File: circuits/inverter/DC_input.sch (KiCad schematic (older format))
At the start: 0 parts

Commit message: Add more circuitry, add library content
AC current measurement
AC filter
AC switch
DC booster
DC input
Analog frontend
drivers
inverter
main controller
power supply

new components for:
standard library (e.g. relay)
AC current sensor acs722
voltage regulator LM317L

Footprints for:
AC relay
TO-220
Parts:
- added C? (x4): Capacitor, symbol Capacitor
- added L? (x2): Inductor, symbol Inductor
- added MB?: DC+_Terminal, symbol Plated_hole
- added MB?: DC-_Terminal, symbol Plated_hole
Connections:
- net labels added: DC+, DC-_Shunt+, Earth_Protective
- wire segments 0 -> 14
- no-connect marks 0 -> 1
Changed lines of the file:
@@
 EESchema Schematic File Version 2
+LIBS:lm317
 LIBS:kv30f
 LIBS:OSSI_standard_components
@@
 LIBS:lm4030
 LIBS:power
+LIBS:acs722
 LIBS:OSSI_MK_I-cache
 EELAYER 25 0
@@
 $Descr A4 11693 8268
 encoding utf-8
-Sheet 1 10
-Title ""
+Sheet 2 11
+Title "DC Input Terminals and Filter"
 Date ""
 Rev "0.1"
@@
 Comment4 ""
 $EndDescr
+$Comp
+L Plated_hole MB?
+U 1 1 56E6DE87
+P 2700 3000
+F 0 "MB?" H 2700 2850 60  0000 C CNN
+F 1 "DC+_Terminal" H 2710 3160 60  0000 C CNN
+F 2 "" H 2700 3000 60  0000 C CNN
+F 3 "" H 2700 3000 60  0000 C CNN
+	1    2700 3000
+	1    0    0    -1
+$EndComp
+$Comp
+L Plated_hole MB?
+U 1 1 56E6DFE4
+P 2700 4150
+F 0 "MB?" H 2700 4000 60  0000 C CNN
+F 1 "DC-_Terminal" H 2710 4310 60  0000 C CNN
+F 2 "" H 2700 4150 60  0000 C CNN
+F 3 "" H 2700 4150 60  0000 C CNN
+	1    2700 4150
+	1    0    0    -1
+$EndComp
+$Comp
+L Capacitor C?
+U 1 1 56E6E0C5
+P 4300 3250
+F 0 "C?" H 4300 3100 60  0000 C CNN
+F 1 "Capacitor" H 4315 3395 60  0000 C CNN
+F 2 "" H 4300 3250 60  0000 C CNN
+F 3 "" H 4300 3250 60  0000 C CNN
+F 4 "%" H 4300 3475 60  0000 C CNN "Tolerance"
+F 5 "M" H 4550 3450 60  0001 L CNN "Manufacturer"
+F 6 "P" H 4550 3350 60  0001 L CNN "Partnumber"
+	1    4300 3250
+	0    -1   1    0
+$EndComp
+$Comp
+L Capacitor C?
+U 1 1 56E6E157
+P 4300 3850
+F 0 "C?" H 4300 3700 60  0000 C CNN
+F 1 "Capacitor" H 4315 3995 60  0000 C CNN
+F 2 "" H 4300 3850 60  0000 C CNN
+F 3 "" H 4300 3850 60  0000 C CNN
+F 4 "%" H 4300 4075 60  0000 C CNN "Tolerance"
+F 5 "M" H 4550 4050 60  0001 L CNN "Manufacturer"
+F 6 "P" H 4550 3950 60  0001 L CNN "Partnumber"
+	1    4300 3850
+	0    -1   1    0
+$EndComp
+$Comp
+L Inductor L?
+U 1 1 56E6E196
+P 5250 3000
+F 0 "L?" H 5250 2850 60  0000 C CNN
+F 1 "Inductor" H 5250 2950 60  0000 C CNN
+F 2 "" H 5250 3000 60  0000 C CNN
+F 3 "" H 5250 3000 60  0000 C CNN
+F 4 "M" H 5425 3200 60  0001 L CNN "Manufacturer"
+F 5 "P" H 5425 3100 60  0001 L CNN "Partnumber"
+	1    5250 3000
+	1    0    0    -1
+$EndComp
+$Comp
+L Inductor L?
+U 1 1 56E6E24A
+P 5250 4150
+F 0 "L?" H 5250 4000 60  0000 C CNN
+F 1 "Inductor" H 5250 4100 60  0000 C CNN
+F 2 "" H 5250 4150 60  0000 C CNN
+F 3 "" H 5250 4150 60  0000 C CNN
+F 4 "M" H 5425 4350 60  0001 L CNN "Manufacturer"
+F 5 "P" H 5425 4250 60  0001 L CNN "Partnumber"
+	1    5250 4150
+	1    0    0    -1
+$EndComp
+$Comp
+L Capacitor C?
+U 1 1 56E6E29F
+P 6250 3250
+F 0 "C?" H 6250 3100 60  0000 C CNN
+F 1 "Capacitor" H 6265 3395 60  0000 C CNN
+F 2 "" H 6250 3250 60  0000 C CNN
+F 3 "" H 6250 3250 60  0000 C CNN
+F 4 "%" H 6250 3475 60  0000 C CNN "Tolerance"
+F 5 "M" H 6500 3450 60  0001 L CNN "Manufacturer"
+F 6 "P" H 6500 3350 60  0001 L CNN "Partnumber"
+	1    6250 3250
+	0    -1   1    0
+$EndComp
+$Comp
+L Capacitor C?
+U 1 1 56E6E320
+P 6250 3800
+F 0 "C?" H 6250 3650 60  0000 C CNN
+F 1 "Capacitor" H 6265 3945 60  0000 C CNN
+F 2 "" H 6250 3800 60  0000 C CNN
+F 3 "" H 6250 3800 60  0000 C CNN
+F 4 "%" H 6250 4025 60  0000 C CNN "Tolerance"
+F 5 "M" H 6500 4000 60  0001 L CNN "Manufacturer"
+F 6 "P" H 6500 3900 60  0001 L CNN "Partnumber"
+	1    6250 3800
+	0    -1   1    0
+$EndComp
+Wire Wire Line
+	2700 4150 5000 4150
+Wire Wire Line
+	5500 4150 8000 4150
+Text HLabel 8000 3000 2    60   Output ~ 0
+DC+
+Wire Wire Line
+	5500 3000 8000 3000
+Wire Wire Line
+	6250 3150 6250 3000
+Connection ~ 6250 3000
+Wire Wire Line
+	6250 3350 6250 3700
+Wire Wire Line
+	6250 3900 6250 4150
+Connection ~ 6250 4150
+Wire Wire Line
+	2700 3000 5000 3000
+Wire Wire Line
+	4300 3150 4300 3000
+Connection ~ 4300 3000
+Wire Wire Line
+	4300 3350 4300 3750
+Wire Wire Line
+	4300 3950 4300 4150
+Connection ~ 4300 4150
+$Comp
+L Earth_Protective #PWR?
+U 1 1 56E6E7AC
+P 4750 3600
+F 0 "#PWR?" H 5000 3350 50  0001 C CNN
+F 1 "Earth_Protective" H 5200 3450 50  0001 C CNN
+F 2 "" H 4750 3500 50  0000 C CNN
+F 3 "" H 4750 3500 50  0000 C CNN
+	1    4750 3600
+	1    0    0    -1
+$EndComp
+Wire Wire Line
+	4750 3600 4750 3550
+Wire Wire Line
+	4750 3550 4300 3550
+Connection ~ 4300 3550
+$Comp
+L Earth_Protective #PWR?
+U 1 1 56E6EC38
+P 6700 3600
+F 0 "#PWR?" H 6950 3350 50  0001 C CNN
+F 1 "Earth_Protective" H 7150 3450 50  0001 C CNN
+F 2 "" H 6700 3500 50  0000 C CNN
+F 3 "" H 6700 3500 50  0000 C CNN
+	1    6700 3600
+	1    0    0    -1
+$EndComp
+Wire Wire Line
+	6700 3600 6700 3550
+Wire Wire Line
+	6700 3550 6250 3550
+Connection ~ 6250 3550
+NoConn ~ 6050 3600
+Text HLabel 8000 4150 2    60   Input ~ 0
+DC-_Shunt+
 $EndSCHEMATC

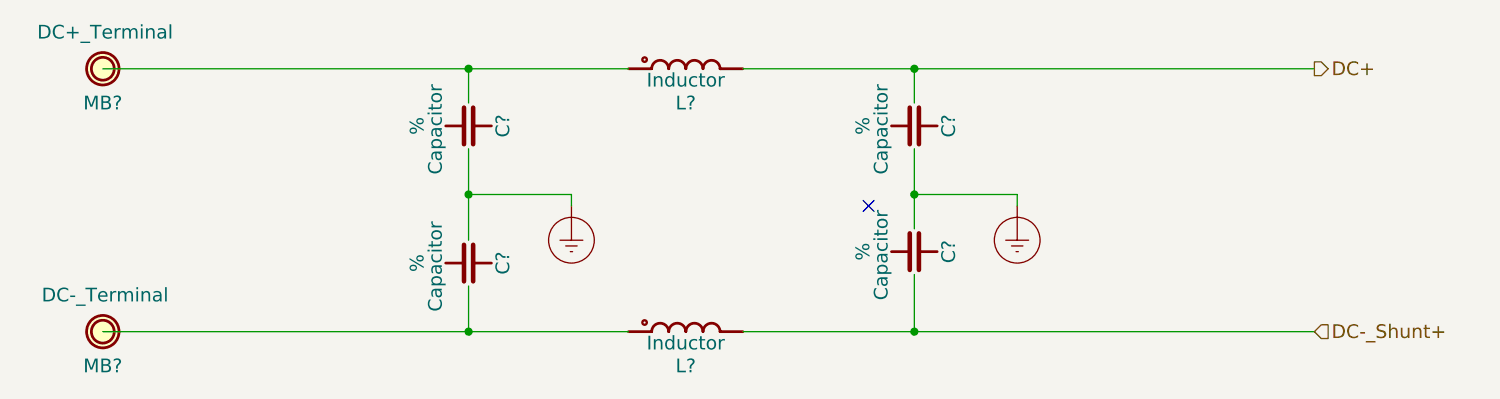
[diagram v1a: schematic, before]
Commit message: Updates all schematic pages to current components
all components are replaced with the current component library parts
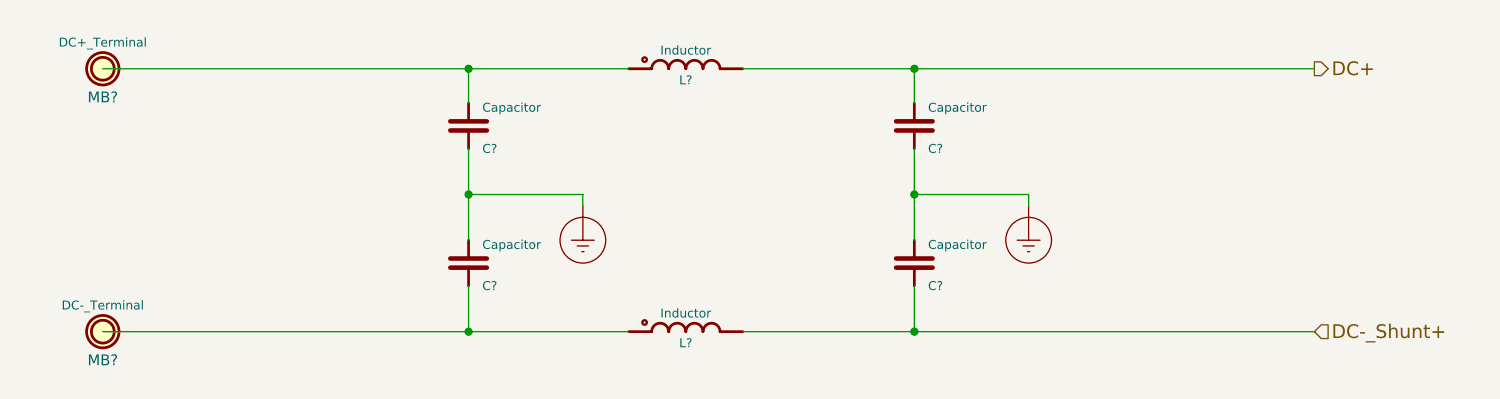
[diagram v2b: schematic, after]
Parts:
- removed C? (x4): Capacitor, symbol Capacitor
- removed L? (x2): Inductor, symbol Inductor
- removed MB?: DC+_Terminal, symbol Plated_hole
- removed MB?: DC-_Terminal, symbol Plated_hole
- added C? (x4): Capacitor, symbol Capacitor
- added L? (x2): Inductor, symbol Inductor
- added MB?: DC+_Terminal, symbol Plated_hole
- added MB?: DC-_Terminal, symbol Plated_hole
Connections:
- wire segments 14 -> 20
- no-connect marks 1 -> 0
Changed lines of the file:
@@
 LIBS:connectors
 LIBS:lm4030
-LIBS:power
 LIBS:acs722
 LIBS:OSSI_MK_I-cache
@@
 Comment4 ""
 $EndDescr
+Wire Wire Line
+	2700 4150 4300 4150
+Wire Wire Line
+	4300 4150 5000 4150
+Wire Wire Line
+	5500 4150 6250 4150
+Wire Wire Line
+	6250 4150 8000 4150
+Text HLabel 8000 3000 2    60   Output ~ 0
+DC+
+Wire Wire Line
+	5500 3000 6250 3000
+Wire Wire Line
+	6250 3000 8000 3000
+Wire Wire Line
+	6250 3150 6250 3000
+Connection ~ 6250 3000
+Wire Wire Line
+	6250 3350 6250 3550
+Wire Wire Line
+	6250 3550 6250 3750
+Wire Wire Line
+	6250 3950 6250 4150
+Connection ~ 6250 4150
+Wire Wire Line
+	2700 3000 4300 3000
+Wire Wire Line
+	4300 3000 5000 3000
+Wire Wire Line
+	4300 3150 4300 3000
+Connection ~ 4300 3000
+Wire Wire Line
+	4300 3350 4300 3550
+Wire Wire Line
+	4300 3550 4300 3750
+Wire Wire Line
+	4300 3950 4300 4150
+Connection ~ 4300 4150
+$Comp
+L Earth_Protective #PWR01
+U 1 1 56E6E7AC
+P 4800 3600
+F 0 "#PWR01" H 5050 3350 50  0001 C CNN
+F 1 "Earth_Protective" H 5250 3450 50  0001 C CNN
+F 2 "" H 4800 3500 50  0000 C CNN
+F 3 "" H 4800 3500 50  0000 C CNN
+	1    4800 3600
+	1    0    0    -1
+$EndComp
+Wire Wire Line
+	4800 3600 4800 3550
+Wire Wire Line
+	4800 3550 4300 3550
+Connection ~ 4300 3550
+$Comp
+L Earth_Protective #PWR02
+U 1 1 56E6EC38
+P 6750 3600
+F 0 "#PWR02" H 7000 3350 50  0001 C CNN
+F 1 "Earth_Protective" H 7200 3450 50  0001 C CNN
+F 2 "" H 6750 3500 50  0000 C CNN
+F 3 "" H 6750 3500 50  0000 C CNN
+	1    6750 3600
+	1    0    0    -1
+$EndComp
+Wire Wire Line
+	6750 3600 6750 3550
+Wire Wire Line
+	6750 3550 6250 3550
+Connection ~ 6250 3550
+Text HLabel 8000 4150 2    60   Input ~ 0
+DC-_Shunt+
+$Comp
+L Capacitor C?
+U 1 1 58D7EC0B
+P 4300 3250
+F 0 "C?" H 4360 3150 39  0000 L CNN
+F 1 "Capacitor" H 4360 3330 39  0000 L CNN
+F 2 "" H 4250 3160 39  0001 R CNN
+F 3 "" V 4300 3250 60  0000 C CNN
+F 4 "%" H 4250 3330 39  0001 R CNN "Tolerance"
+F 5 "M" H 4360 3445 35  0001 L CNN "Manufacturer"
+F 6 "P" H 4360 3390 35  0001 L CNN "Partnumber"
+F 7 "S" H 4360 3505 35  0001 L CNN "Supplier"
+F 8 "O.No." H 4360 3555 35  0001 L CNN "Order No."
+	1    4300 3250
+	1    0    0    -1
+$EndComp
+$Comp
+L Capacitor C?
+U 1 1 58D7EC75
+P 4300 3850
+F 0 "C?" H 4360 3750 39  0000 L CNN
+F 1 "Capacitor" H 4360 3930 39  0000 L CNN
+F 2 "" H 4250 3760 39  0001 R CNN
+F 3 "" V 4300 3850 60  0000 C CNN
+F 4 "%" H 4250 3930 39  0001 R CNN "Tolerance"
+F 5 "M" H 4360 4045 35  0001 L CNN "Manufacturer"
+F 6 "P" H 4360 3990 35  0001 L CNN "Partnumber"
+F 7 "S" H 4360 4105 35  0001 L CNN "Supplier"
+F 8 "O.No." H 4360 4155 35  0001 L CNN "Order No."
+	1    4300 3850
+	1    0    0    -1
+$EndComp
+$Comp
+L Capacitor C?
+U 1 1 58D7ED36
+P 6250 3250
+F 0 "C?" H 6310 3150 39  0000 L CNN
+F 1 "Capacitor" H 6310 3330 39  0000 L CNN
+F 2 "" H 6200 3160 39  0001 R CNN
+F 3 "" V 6250 3250 60  0000 C CNN
+F 4 "%" H 6200 3330 39  0001 R CNN "Tolerance"
+F 5 "M" H 6310 3445 35  0001 L CNN "Manufacturer"
+F 6 "P" H 6310 3390 35  0001 L CNN "Partnumber"
+F 7 "S" H 6310 3505 35  0001 L CNN "Supplier"
+F 8 "O.No." H 6310 3555 35  0001 L CNN "Order No."
+	1    6250 3250
+	1    0    0    -1
+$EndComp
+$Comp
+L Capacitor C?
+U 1 1 58D7EDAD
+P 6250 3850
+F 0 "C?" H 6310 3750 39  0000 L CNN
+F 1 "Capacitor" H 6310 3930 39  0000 L CNN
+F 2 "" H 6200 3760 39  0001 R CNN
+F 3 "" V 6250 3850 60  0000 C CNN
+F 4 "%" H 6200 3930 39  0001 R CNN "Tolerance"
+F 5 "M" H 6310 4045 35  0001 L CNN "Manufacturer"
+F 6 "P" H 6310 3990 35  0001 L CNN "Partnumber"
+F 7 "S" H 6310 4105 35  0001 L CNN "Supplier"
+F 8 "O.No." H 6310 4155 35  0001 L CNN "Order No."
+	1    6250 3850
+	1    0    0    -1
+$EndComp
+$Comp
+L Inductor L?
+U 1 1 58D7EE81
+P 5250 3000
+F 0 "L?" H 5250 2950 39  0000 C CNN
+F 1 "Inductor" H 5250 3080 39  0000 C CNN
+F 2 "" H 5250 3155 35  0000 C CNN
+F 3 "" H 5250 3000 60  0000 C CNN
+F 4 "M" H 5420 3185 35  0001 L CNN "Manufacturer"
+F 5 "P" H 5420 3130 35  0001 L CNN "Partnumber"
+F 6 "S" H 5420 3240 35  0001 L CNN "Supplier"
+F 7 "O.No." H 5420 3290 35  0001 L CNN "Order No."
+	1    5250 3000
+	1    0    0    -1
+$EndComp
+$Comp
+L Inductor L?
+U 1 1 58D7EEE9
+P 5250 4150
+F 0 "L?" H 5250 4100 39  0000 C CNN
+F 1 "Inductor" H 5250 4230 39  0000 C CNN
+F 2 "" H 5250 4305 35  0000 C CNN
+F 3 "" H 5250 4150 60  0000 C CNN
+F 4 "M" H 5420 4335 35  0001 L CNN "Manufacturer"
+F 5 "P" H 5420 4280 35  0001 L CNN "Partnumber"
+F 6 "S" H 5420 4390 35  0001 L CNN "Supplier"
+F 7 "O.No." H 5420 4440 35  0001 L CNN "Order No."
+	1    5250 4150
+	1    0    0    -1
+$EndComp
 $Comp
 L Plated_hole MB?
-U 1 1 56E6DE87
+U 1 1 58E38B7C
 P 2700 3000
-F 0 "MB?" H 2700 2850 60  0000 C CNN
-F 1 "DC+_Terminal" H 2710 3160 60  0000 C CNN
+F 0 "MB?" H 2700 2875 47  0000 C CNN
+F 1 "DC+_Terminal" H 2700 3115 39  0000 C CNN
 F 2 "" H 2700 3000 60  0000 C CNN
 F 3 "" H 2700 3000 60  0000 C CNN
@@
 $Comp
 L Plated_hole MB?
-U 1 1 56E6DFE4
+U 1 1 58E38E08
 P 2700 4150
-F 0 "MB?" H 2700 4000 60  0000 C CNN
-F 1 "DC-_Terminal" H 2710 4310 60  0000 C CNN
+F 0 "MB?" H 2700 4025 47  0000 C CNN
+F 1 "DC-_Terminal" H 2700 4265 39  0000 C CNN
 F 2 "" H 2700 4150 60  0000 C CNN
 F 3 "" H 2700 4150 60  0000 C CNN
@@
 	1    0    0    -1
 $EndComp
-$Comp
-L Capacitor C?
-U 1 1 56E6E0C5
-P 4300 3250
-F 0 "C?" H 4300 3100 60  0000 C CNN
-F 1 "Capacitor" H 4315 3395 60  0000 C CNN
-F 2 "" H 4300 3250 60  0000 C CNN
-F 3 "" H 4300 3250 60  0000 C CNN
-F 4 "%" H 4300 3475 60  0000 C CNN "Tolerance"
-F 5 "M" H 4550 3450 60  0001 L CNN "Manufacturer"
-F 6 "P" H 4550 3350 60  0001 L CNN "Partnumber"
-	1    4300 3250
-	0    -1   1    0
-$EndComp
-$Comp
-L Capacitor C?
-U 1 1 56E6E157
-P 4300 3850
-F 0 "C?" H 4300 3700 60  0000 C CNN
-F 1 "Capacitor" H 4315 3995 60  0000 C CNN
-F 2 "" H 4300 3850 60  0000 C CNN
-F 3 "" H 4300 3850 60  0000 C CNN
-F 4 "%" H 4300 4075 60  0000 C CNN "Tolerance"
-F 5 "M" H 4550 4050 60  0001 L CNN "Manufacturer"
-F 6 "P" H 4550 3950 60  0001 L CNN "Partnumber"
-	1    4300 3850
-	0    -1   1    0
-$EndComp
-$Comp
-L Inductor L?
-U 1 1 56E6E196
-P 5250 3000
-F 0 "L?" H 5250 2850 60  0000 C CNN
-F 1 "Inductor" H 5250 2950 60  0000 C CNN
-F 2 "" H 5250 3000 60  0000 C CNN
-F 3 "" H 5250 3000 60  0000 C CNN
-F 4 "M" H 5425 3200 60  0001 L CNN "Manufacturer"
-F 5 "P" H 5425 3100 60  0001 L CNN "Partnumber"
-	1    5250 3000
-	1    0    0    -1
-$EndComp
-$Comp
-L Inductor L?
-U 1 1 56E6E24A
-P 5250 4150
-F 0 "L?" H 5250 4000 60  0000 C CNN
-F 1 "Inductor" H 5250 4100 60  0000 C CNN
-F 2 "" H 5250 4150 60  0000 C CNN
-F 3 "" H 5250 4150 60  0000 C CNN
-F 4 "M" H 5425 4350 60  0001 L CNN "Manufacturer"
-F 5 "P" H 5425 4250 60  0001 L CNN "Partnumber"
-	1    5250 4150
-	1    0    0    -1
-$EndComp
-$Comp
-L Capacitor C?
-U 1 1 56E6E29F
-P 6250 3250
-F 0 "C?" H 6250 3100 60  0000 C CNN
-F 1 "Capacitor" H 6265 3395 60  0000 C CNN
-F 2 "" H 6250 3250 60  0000 C CNN
-F 3 "" H 6250 3250 60  0000 C CNN
-F 4 "%" H 6250 3475 60  0000 C CNN "Tolerance"
-F 5 "M" H 6500 3450 60  0001 L CNN "Manufacturer"
-F 6 "P" H 6500 3350 60  0001 L CNN "Partnumber"
-	1    6250 3250
-	0    -1   1    0
-$EndComp
-$Comp
-L Capacitor C?
-U 1 1 56E6E320
-P 6250 3800
-F 0 "C?" H 6250 3650 60  0000 C CNN
-F 1 "Capacitor" H 6265 3945 60  0000 C CNN
-F 2 "" H 6250 3800 60  0000 C CNN
-F 3 "" H 6250 3800 60  0000 C CNN
-F 4 "%" H 6250 4025 60  0000 C CNN "Tolerance"
-F 5 "M" H 6500 4000 60  0001 L CNN "Manufacturer"
-F 6 "P" H 6500 3900 60  0001 L CNN "Partnumber"
-	1    6250 3800
-	0    -1   1    0
-$EndComp
-Wire Wire Line
-	2700 4150 5000 4150
-Wire Wire Line
-	5500 4150 8000 4150
-Text HLabel 8000 3000 2    60   Output ~ 0
-DC+
-Wire Wire Line
-	5500 3000 8000 3000
-Wire Wire Line
-	6250 3150 6250 3000
-Connection ~ 6250 3000
-Wire Wire Line
-	6250 3350 6250 3700
-Wire Wire Line
-	6250 3900 6250 4150
-Connection ~ 6250 4150
-Wire Wire Line
-	2700 3000 5000 3000
-Wire Wire Line
-	4300 3150 4300 3000
-Connection ~ 4300 3000
-Wire Wire Line
-	4300 3350 4300 3750
-Wire Wire Line
-	4300 3950 4300 4150
-Connection ~ 4300 4150
-$Comp
-L Earth_Protective #PWR?
-U 1 1 56E6E7AC
-P 4750 3600
-F 0 "#PWR?" H 5000 3350 50  0001 C CNN
-F 1 "Earth_Protective" H 5200 3450 50  0001 C CNN
-F 2 "" H 4750 3500 50  0000 C CNN
-F 3 "" H 4750 3500 50  0000 C CNN
-	1    4750 3600
-	1    0    0    -1
-$EndComp
-Wire Wire Line
-	4750 3600 4750 3550
-Wire Wire Line
-	4750 3550 4300 3550
-Connection ~ 4300 3550
-$Comp
-L Earth_Protective #PWR?
-U 1 1 56E6EC38
-P 6700 3600
-F 0 "#PWR?" H 6950 3350 50  0001 C CNN
-F 1 "Earth_Protective" H 7150 3450 50  0001 C CNN
-F 2 "" H 6700 3500 50  0000 C CNN
-F 3 "" H 6700 3500 50  0000 C CNN
-	1    6700 3600
-	1    0    0    -1
-$EndComp
-Wire Wire Line
-	6700 3600 6700 3550
-Wire Wire Line
-	6700 3550 6250 3550
-Connection ~ 6250 3550
-NoConn ~ 6050 3600
-Text HLabel 8000 4150 2    60   Input ~ 0
-DC-_Shunt+
 $EndSCHEMATC

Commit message: bulk-updates libraries and schematics
schematic is updated to Kicad 5.1.14
updates various sheets with new circuits
adds various component libraries
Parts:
- removed L? (x2): Inductor, symbol Inductor
- added L?: Choke_cc, symbol OSSI_standard_components:Choke_cc
- C? (x4): symbol Capacitor -> OSSI_standard_components:Capacitor
- MB? (x2): symbol Plated_hole -> OSSI_standard_components:Plated_hole
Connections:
- net DC+: now also L?.1B
- net DC-_Shunt+: now also L?.2B
- net at C?.2, MB?.1: now also L?.1A
- net at C?.1, MB?.1: now also L?.2A
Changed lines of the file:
@@
-EESchema Schematic File Version 2
-LIBS:lm317
-LIBS:kv30f
-LIBS:OSSI_standard_components
-LIBS:connectors
-LIBS:lm4030
-LIBS:acs722
+EESchema Schematic File Version 4
 LIBS:OSSI_MK_I-cache
-EELAYER 25 0
+EELAYER 30 0
 EELAYER END
 $Descr A4 11693 8268
@@
 	4300 4150 5000 4150
 Wire Wire Line
-	5500 4150 6250 4150
-Wire Wire Line
 	6250 4150 8000 4150
 Text HLabel 8000 3000 2    60   Output ~ 0
 DC+
 Wire Wire Line
-	5500 3000 6250 3000
-Wire Wire Line
 	6250 3000 8000 3000
 Wire Wire Line
@@
 Connection ~ 4300 4150
 $Comp
-L Earth_Protective #PWR01
+L OSSI_standard_components:Earth_Protective #PWR01
 U 1 1 56E6E7AC
 P 4800 3600
@@
 Connection ~ 4300 3550
 $Comp
-L Earth_Protective #PWR02
+L OSSI_standard_components:Earth_Protective #PWR02
 U 1 1 56E6EC38
 P 6750 3600
@@
 DC-_Shunt+
 $Comp
-L Capacitor C?
+L OSSI_standard_components:Capacitor C?
 U 1 1 58D7EC0B
 P 4300 3250
@@
 $EndComp
 $Comp
-L Capacitor C?
+L OSSI_standard_components:Capacitor C?
 U 1 1 58D7EC75
 P 4300 3850
@@
 $EndComp
 $Comp
-L Capacitor C?
+L OSSI_standard_components:Capacitor C?
 U 1 1 58D7ED36
 P 6250 3250
@@
 $EndComp
 $Comp
-L Capacitor C?
+L OSSI_standard_components:Capacitor C?
 U 1 1 58D7EDAD
 P 6250 3850
@@
 $EndComp
 $Comp
-L Inductor L?
-U 1 1 58D7EE81
-P 5250 3000
-F 0 "L?" H 5250 2950 39  0000 C CNN
-F 1 "Inductor" H 5250 3080 39  0000 C CNN
-F 2 "" H 5250 3155 35  0000 C CNN
-F 3 "" H 5250 3000 60  0000 C CNN
-F 4 "M" H 5420 3185 35  0001 L CNN "Manufacturer"
-F 5 "P" H 5420 3130 35  0001 L CNN "Partnumber"
-F 6 "S" H 5420 3240 35  0001 L CNN "Supplier"
-F 7 "O.No." H 5420 3290 35  0001 L CNN "Order No."
-	1    5250 3000
-	1    0    0    -1
-$EndComp
-$Comp
-L Inductor L?
-U 1 1 58D7EEE9
-P 5250 4150
-F 0 "L?" H 5250 4100 39  0000 C CNN
-F 1 "Inductor" H 5250 4230 39  0000 C CNN
-F 2 "" H 5250 4305 35  0000 C CNN
-F 3 "" H 5250 4150 60  0000 C CNN
-F 4 "M" H 5420 4335 35  0001 L CNN "Manufacturer"
-F 5 "P" H 5420 4280 35  0001 L CNN "Partnumber"
-F 6 "S" H 5420 4390 35  0001 L CNN "Supplier"
-F 7 "O.No." H 5420 4440 35  0001 L CNN "Order No."
-	1    5250 4150
-	1    0    0    -1
-$EndComp
-$Comp
-L Plated_hole MB?
+L OSSI_standard_components:Plated_hole MB?
 U 1 1 58E38B7C
 P 2700 3000
@@
 $EndComp
 $Comp
-L Plated_hole MB?
+L OSSI_standard_components:Plated_hole MB?
 U 1 1 58E38E08
 P 2700 4150
@@
 	1    0    0    -1
 $EndComp
+$Comp
+L OSSI_standard_components:Choke_cc L?
+U 1 1 5B6F27F9
+P 5400 3550
+F 0 "L?" H 5400 3400 39  0000 C CNN
+F 1 "Choke_cc" H 5400 3729 39  0000 C CNN
+F 2 "" H 5400 3705 35  0000 C CNN
+F 3 "" H 5400 3450 60  0000 C CNN
+F 4 "M" H 5570 3785 35  0001 L CNN "Manufacturer"
+F 5 "P" H 5570 3730 35  0001 L CNN "Partnumber"
+F 6 "S" H 5570 3840 35  0001 L CNN "Supplier"
+F 7 "O.No." H 5570 3890 35  0001 L CNN "Order No."
+	1    5400 3550
+	1    0    0    -1
+$EndComp
+Wire Wire Line
+	5650 3450 5750 3450
+Wire Wire Line
+	5750 3450 5750 3000
+Wire Wire Line
+	5750 3000 6250 3000
+Wire Wire Line
+	5650 3650 5750 3650
+Wire Wire Line
+	5750 3650 5750 4150
+Wire Wire Line
+	5750 4150 6250 4150
+Wire Wire Line
+	5000 3650 5150 3650
+Wire Wire Line
+	5000 3000 5000 3450
+Wire Wire Line
+	5000 3450 5150 3450
+Wire Wire Line
+	5000 3650 5000 4150
 $EndSCHEMATC
